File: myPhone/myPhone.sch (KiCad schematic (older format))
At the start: 135 parts, among them J1 USB_OTG, J2 BATT, J3 RV.Debug, J4 SJ-3571N, J5 Display, J6 Touch, Q1 MMBT3906, SW1 RESET, SW2 WAKE, U1 BQ25895, U10 74HC595, U11 ICS-43434, U12 MAX98357A, U13 FT813Q, U14 FAN5333BSX, U2 TPS62293, U3 TPS630250, U4 SN74LVC2G07, U5 E310-G000, U6 IS25LP128-JBLE, U7 74HC00, U8 74HC00, U9 74HC595, X1 SiT1533, Y1 16MHz, Y2 12MHz

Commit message: upgrade to kicad 5; fixed footprints
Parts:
- removed J1: USB_OTG, footprints:USB_Micro-B, symbol USB_OTG
- removed J2: BATT, Pin_Headers:Pin_Header_Straight_1x02_Pitch2.00mm, symbol Conn_01x02
- removed J3: RV.Debug, Pin_Headers:Pin_Header_Straight_1x06_Pitch2.54mm, symbol Conn_01x06
- removed J5: Display, footprints:Hirose_FH12-40S-0.5SH_1x40-1MP_P0.50mm_Horizontal_Bottom, symbol Conn_01x40
- removed J6: Touch, footprints:Hirose_FH12-6S-0.5SH_1x06-1MP_P0.50mm_Horizontal_Bottom, symbol Conn_01x06
- removed Q1: MMBT3906, TO_SOT_Packages_SMD:SOT-23, symbol MMBT3906
- removed SW1: RESET, footprints:Panasonic_EVPBB, symbol SW_Push
- removed SW2: WAKE, footprints:Panasonic_EVPAK, symbol SW_Push
- removed U10, U9: 74HC595, Housings_SOIC:SOIC-16_3.9x9.9mm_Pitch1.27mm, symbol 74HC595
- removed U7, U8: 74HC00, Housings_SOIC:SOIC-14_3.9x8.7mm_Pitch1.27mm, symbol 74HC00
- added J1: USB_OTG, footprints:USB_Micro-B, symbol Connector:USB_B_Micro
- added J2: BATT, Connector_PinHeader_2.00mm:PinHeader_1x02_P2.00mm_Vertical, symbol Connector_Generic:Conn_01x02
- added J3: RV.Debug, Connector_PinHeader_2.54mm:PinHeader_1x06_P2.54mm_Vertical, symbol Connector_Generic:Conn_01x06
- added J5: Display, footprints:Hirose_FH12-40S-0.5SH_1x40-1MP_P0.50mm_Horizontal_Bottom, symbol Connector_Generic:Conn_01x40
- added J6: Touch, footprints:Hirose_FH12-6S-0.5SH_1x06-1MP_P0.50mm_Horizontal_Bottom, symbol Connector_Generic:Conn_01x06
- added Q1: MMBT3906, Package_TO_SOT_SMD:SOT-23, symbol Transistor_BJT:MMBT3906
- added SW1: RESET, footprints:Panasonic_EVPBB, symbol Switch:SW_Push
- added SW2: WAKE, footprints:Panasonic_EVPAK, symbol Switch:SW_Push
- added U10, U9: 74HC595, Package_SO:SOIC-16_3.9x9.9mm_P1.27mm, symbol 74xx:74HC595
- added U7, U8: 74HC00, Package_SO:SOIC-14_3.9x8.7mm_P1.27mm, symbol 74xx:74HC00
- BZ1: symbol Buzzer -> Device:Buzzer
- C1, C10, C11, C2, C29, C3, C30, C31, C32, C33, C34, C35, C36, C37, C4, C48, C49, C5, C50, C51, C52, C53, C54, C6, C7, C8, C9: footprint Capacitors_SMD:C_0603 -> Capacitor_SMD:C_0603_1608Metric; symbol C -> Device:C
- C12, C13, C14, C15, C16, C17, C18, C19, C20, C21, C22, C23, C24, C25, C26, C27, C28, C38, C39, C40, C41, C42, C43, C44, C45, C46, C47: footprint Capacitors_SMD:C_0603 -> Capacitor_SMD:C_0603_1608Metric; symbol C_Small -> Device:C_Small
- D1: footprint LEDs:LED_0603 -> LED_SMD:LED_0603_1608Metric; symbol LED -> Device:LED
- D2: footprint Diodes_SMD:D_SOD-123 -> Diode_SMD:D_SOD-123; symbol D_Schottky -> Device:D_Schottky
- D3: footprint footprints:DO-214AC -> Diode_SMD:D_SMA; symbol D_Zener -> Device:D_Zener
- J4: symbol SJ-3571N -> cui-sj:SJ-3571N
- JP1, JP2, JP3: footprint Pin_Headers:Pin_Header_Straight_1x02_Pitch1.27mm -> Connector_PinHeader_1.27mm:PinHeader_1x02_P1.27mm_Vertical; symbol Jumper -> Device:Jumper
- L1, L2: footprint footprints:Coilcraft_LPS3015 -> footprints:L_Coilcraft_LPS3015; symbol L -> Device:L
- L3: footprint footprints:Coilcraft_XAL40 -> footprints:L_Coilcraft_XAL40; symbol L -> Device:L
- L4: footprint footprints:Murata_LQH66SN -> footprints:L_Murata_LQH66SN; symbol L -> Device:L
- LS1: footprint Pin_Headers:Pin_Header_Straight_1x02_Pitch1.27mm -> Connector_PinHeader_1.27mm:PinHeader_1x02_P1.27mm_Vertical; symbol Speaker -> Device:Speaker
- R1, R10, R11, R12, R13, R14, R15, R16, R17, R18, R19, R2, R20, R21, R22, R23, R24, R25, R26, R27, R28, R29, R3, R31, R32, R33, R34, R35, R4, R5, R6, R7, R8, R9: footprint Resistors_SMD:R_0603 -> Resistor_SMD:R_0603_1608Metric; symbol R -> Device:R
- R30: footprint Resistors_SMD:R_0603 -> Resistor_SMD:R_0603_1608Metric; symbol R_Small -> Device:R_Small
- RN1, RN2, RN3, RN4, RN5, RN6, RN7, RN8: symbol R_Pack04 -> Device:R_Pack04
- U1: footprint footprints:QFN-24-1EP_4x4mm_Pitch0.5mm -> Package_DFN_QFN:Texas_S-PWQFN-N24_EP2.7x2.7mm_ThermalVias; symbol BQ25895 -> texas-tps:BQ25895
- U11: symbol ICS-43434 -> ics-43434:ICS-43434
- U12: footprint footprints:MAX98357 -> Package_DFN_QFN:TQFN-16-1EP_3x3mm_P0.5mm_EP1.23x1.23mm; symbol MAX98357 -> max98357:MAX98357
- U13: footprint footprints:FT813Q -> Package_DFN_QFN:QFN-56-1EP_8x8mm_P0.5mm_EP5.6x5.6mm_ThermalVias; symbol FT813Q -> ft81x:FT813Q
- U14: footprint TO_SOT_Packages_SMD:SOT-23-5 -> Package_TO_SOT_SMD:SOT-23-5; symbol FAN5333 -> fan5333:FAN5333
- U2: symbol TPS62290 -> texas-tps:TPS62290
- U3: symbol TPS630250 -> texas-tps:TPS630250
- U4: footprint TO_SOT_Packages_SMD:SC-70-6 -> Package_TO_SOT_SMD:SOT-363_SC-70-6; symbol SN74LVC2G07 -> sn74:SN74LVC2G07
- U5: footprint Housings_DFN_QFN:UQFN-48-1EP_6x6mm_Pitch0.4mm -> Package_DFN_QFN:QFN-48-1EP_6x6mm_P0.4mm_EP4.2x4.2mm_ThermalVias; symbol E310-G000 -> e310-g000:E310-G000
- U6: footprint Housings_SOIC:SOIJ-8_5.3x5.3mm_Pitch1.27mm -> Package_SO:SOIJ-8_5.3x5.3mm_P1.27mm; symbol IS25LP128 -> is25lp128:IS25LP128
- X1: symbol SiT1533 -> sit1533:SiT1533
- Y1, Y2: symbol Crystal_GND3_Small -> Device:Crystal_GND3_Small
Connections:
- wire segments 582 -> 778
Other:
- moved on the sheet: BZ1, C29, C30, C31, C32, C33, C34, C35, C36, C37, R15, R16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

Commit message: REV1 board
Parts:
- removed C15: 0.1uF, Capacitor_SMD:C_0603_1608Metric, symbol Device:C_Small
- removed J3: RV.Debug, Connector_PinHeader_2.54mm:PinHeader_1x06_P2.54mm_Vertical, symbol Connector_Generic:Conn_01x06
- removed J5: Display, footprints:Hirose_FH12-40S-0.5SH_1x40-1MP_P0.50mm_Horizontal_Bottom, symbol Connector_Generic:Conn_01x40
- removed J6: Touch, footprints:Hirose_FH12-6S-0.5SH_1x06-1MP_P0.50mm_Horizontal_Bottom, symbol Connector_Generic:Conn_01x06
- removed R30: 33R, Resistor_SMD:R_0603_1608Metric, symbol Device:R_Small
- removed R31: 4.7K, Resistor_SMD:R_0603_1608Metric, symbol Device:R
- removed R32, R33: 1K, Resistor_SMD:R_0603_1608Metric, symbol Device:R
- removed R34: 100K, Resistor_SMD:R_0603_1608Metric, symbol Device:R
- removed RN1, RN2, RN3, RN4, RN5, RN6, RN7, RN8: 33R, footprints:R_Array_Convex_4x0402, symbol Device:R_Pack04
- removed U4: SN74LVC2G07, Package_TO_SOT_SMD:SOT-363_SC-70-6, symbol sn74:SN74LVC2G07
- removed U5: E310-G000, Package_DFN_QFN:QFN-48-1EP_6x6mm_P0.4mm_EP4.2x4.2mm_ThermalVias, symbol e310-g000:E310-G000
- added R36: 100K, Resistor_SMD:R_0603_1608Metric, symbol Device:R
- added U5: E310-G002, Package_DFN_QFN:QFN-48-1EP_6x6mm_P0.4mm_EP4.2x4.2mm_ThermalVias, symbol e310-g000:E310-G002
- U10, U9: footprint Package_SO:SOIC-16_3.9x9.9mm_P1.27mm -> footprints:74HC595BQ115
- U12: footprint Package_DFN_QFN:TQFN-16-1EP_3x3mm_P0.5mm_EP1.23x1.23mm -> footprints:TQFN-16-1EP_3x3mm_P0.5mm_EP1.23x1.23mm_ThermalVias
- U7, U8: footprint Package_SO:SOIC-14_3.9x8.7mm_P1.27mm -> footprints:74HC00BQ115
- renumbered C20 to C19, C22 to C20, C23 to C21, C19 to C22, C21 to C23, J4 to J3
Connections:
- net +1V8: now also R12.1, U5.30 (VDD), U5.46 (VDD), U5.6 (VDD); no longer C12.1, C19.1, C23.1, R10.2, R11.2, R12.2, X1.4 (VCC)
- net +3V3: now also C12.1, C19.1, C23.1, R10.2, R11.2, X1.4 (VCC), R36.1, U5.11 (IVDD), U5.12 (OTP_AIVDD), U5.19 (AON_IVDD), U5.23 (AON_VDD), U5.32 (IVDD), U5.47 (IVDD)
- net BL_PWM: no longer U13.28 (BL_PWM)
- net GND: now also U5.21 (AON_PSD_LFCLKSEL), U5.49 (GND)
- net GPIO_0: now also U5.25 (GPIO_0/PWM0.0)
- net GPIO_13: now also U5.37 (GPIO_13/PWM2.3)
- net GPIO_18: now also U5.40 (GPIO_18)
- net GPIO_20: now also U5.42 (GPIO_20/PWM1.0)
- net GPIO_21: now also U5.43 (GPIO_21/PWM1.2)
- net GPIO_22: now also U5.44 (GPIO_22/PWM1.3)
- net GPIO_23: now also U5.45 (GPIO_23)
- net JTAG_TCK: now also U5.13 (JTAG_TCK)
- net JTAG_TDI: now also U5.16 (JTAG_TDI)
- net JTAG_TDO: now also U5.14 (JTAG_TDO)
- net JTAG_TMS: now also U5.15 (JTAG_TMS)
- net PWM0.1: now also U5.26 (GPIO_1/PWM0.1)
- net PWM1.1: now also U5.41 (GPIO_19/PWM1.1)
- net PWM2.1: now also U5.35 (GPIO_11/PWM2.1)
- net PWM2.2: now also U5.36 (GPIO_12/PWM2.2)
- net RESET: now also C13.1, R10.1, SW1.2, U5.24 (AON_ERST_N)
- net SPI1.MISO: now also U5.29 (GPIO_4/SPI1.MISO)
- net SPI1.MOSI: now also U5.28 (GPIO_3/SPI1.MOSI/PWM0.3)
- net SPI1.SCK: now also U5.31 (GPIO_5/SPI1.SCK)
- net SPI1.SS0: now also U5.27 (GPIO_2/SPI1.SS0/PWM0.2)
- net SPI1.SS2: now also U5.33 (GPIO_9/SPI1.SS2)
- net SPI1.SS3: now also U5.34 (GPIO_10/SPI1.SS3/PWM2.0)
- net UART0.RX: now also U5.38 (GPIO_16/UART0.RX)
- net UART0.TX: now also U5.39 (GPIO_17/UART0.TX)
- net WAKE: now also C14.1, R11.1, SW2.1, U5.18 (AON_PMU_DWAKEUP_N)
- net XTAL_XO: now reaches C28.1, Y1.2
- net XTAL_XO: now also U5.10 (16M_XTAL_XO)
- net XTAL_XI: now reaches C27.1, Y1.1
- net XTAL_XI: now also U5.9 (16M_XTAL_XI)
- net PLL_AVDD: now reaches C25.1, C26.1
- net PLL_AVDD: now also R12.2, U5.7 (PLL_AVDD); no longer R12.1
- net PLL_AVSS: now reaches C25.2, C26.2
- net PLL_AVSS: now also U5.8 (PLL_AVSS)
- net QSPI_CS: now reaches R35.2, U6.1 (S#)
- net QSPI_CS: now also U5.5 (QSPI_CS)
- net QSPI_DQ_1: now reaches U6.2 (MISO/IO1)
- net QSPI_DQ_1: now also U5.3 (QSPI_DQ_1)
- net QSPI_DQ_2: now reaches U6.3 (WP#/IO2)
- net QSPI_DQ_2: now also U5.2 (QSPI_DQ_2)
- net QSPI_DQ_0: now reaches U6.5 (MOSI/IO0)
- net QSPI_DQ_0: now also U5.4 (QSPI_DQ_0)
- net QSPI_CLK: now reaches U6.6 (SCK)
- net QSPI_CLK: now also U5.48 (QSPI_CLK)
- net QSPI_DQ_3: now reaches U6.7 (HOLD#/IO3)
- net QSPI_DQ_3: now also R36.2, U5.1 (QSPI_DQ_3)
- net PSD_LFALTCLK: now reaches X1.3 (CLKOUT)
- net PSD_LFALTCLK: now also U5.20 (AON_PSD_LFALTCLK)
- net FT813_R0: now reaches U13.2 (R0)
- net FT813_R1: now reaches U13.1 (R1)
- net FT813_R2: now reaches U13.56 (R2)
- net FT813_R3: now reaches U13.55 (R3)
- net FT813_R4: now reaches U13.54 (R4)
- net FT813_R5: now reaches U13.53 (R5)
- net FT813_R6: now reaches U13.52 (R6)
- net FT813_R7: now reaches U13.51 (R7)
- net FT813_G0: now reaches U13.50 (G0)
- net FT813_G1: now reaches U13.49 (G1)
- net FT813_G2: now reaches U13.48 (G2)
- net FT813_G3: now reaches U13.47 (G3)
- net FT813_G4: now reaches U13.46 (G4)
- net FT813_G5: now reaches U13.45 (G5)
- net FT813_G6: now reaches U13.44 (G6)
- net FT813_G7: now reaches U13.43 (G7)
- net FT813_B0: now reaches U13.41 (B0)
- net FT813_B1: now reaches U13.40 (B1)
- net FT813_B2: now reaches U13.39 (B2)
- net FT813_B3: now reaches U13.38 (B3)
- net FT813_B4: now reaches U13.37 (B4)
- net FT813_B5: now reaches U13.36 (B5)
- net FT813_B6: now reaches U13.35 (B6)
- net FT813_B7: now reaches U13.34 (B7)
- net FT813_DISP: now reaches U13.32 (DISP)
- net FT813_HSYNC: now reaches U13.31 (HSYNC)
- net FT813_VSYNC: now reaches U13.30 (VSYNC)
- net FT813_DE: now reaches U13.29 (DE)
- net FT813_PCLK: now reaches U13.33 (PCLK)
- net CTP_INT renamed FT813_CTP_INT
- net CTP_RST renamed FT813_CTP_RST
- net CTP_SCL renamed FT813_CTP_SCL
- net CTP_SDA renamed FT813_CTP_SDA
- new net FT813_BL_PWM: U13.28 (BL_PWM)
- no-connect marks 33 -> 28
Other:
- moved on the sheet: BZ1, C10, C11, C12, C13, C14, C16, C17, C18, C19, C20, C21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

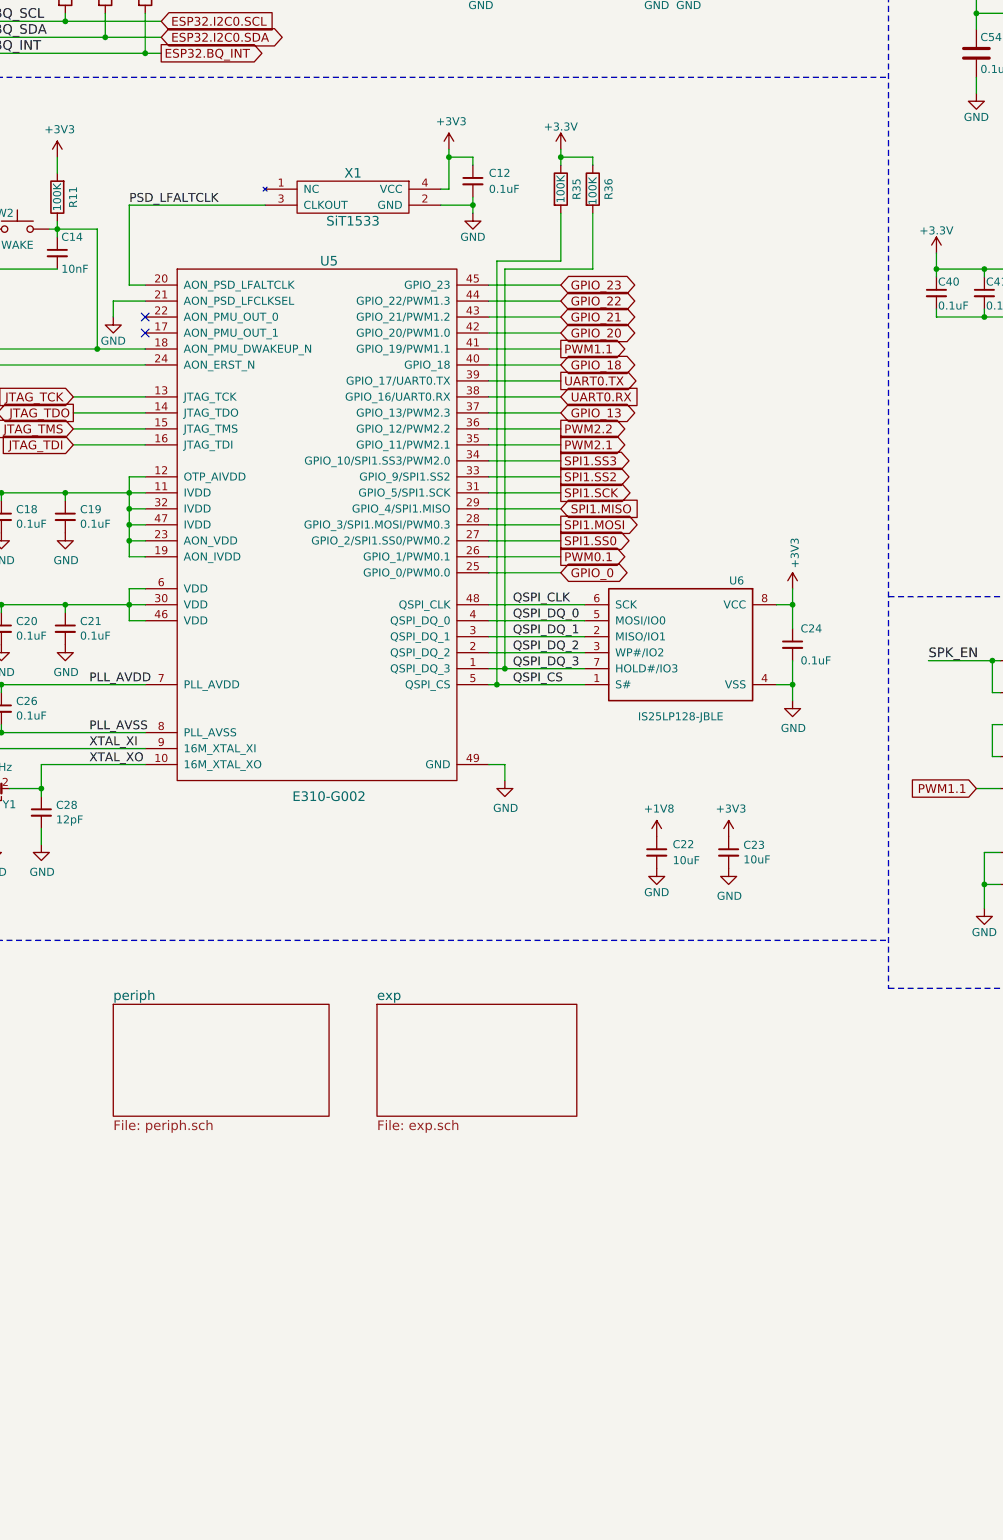
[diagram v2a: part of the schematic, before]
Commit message: display switch pull resistors added
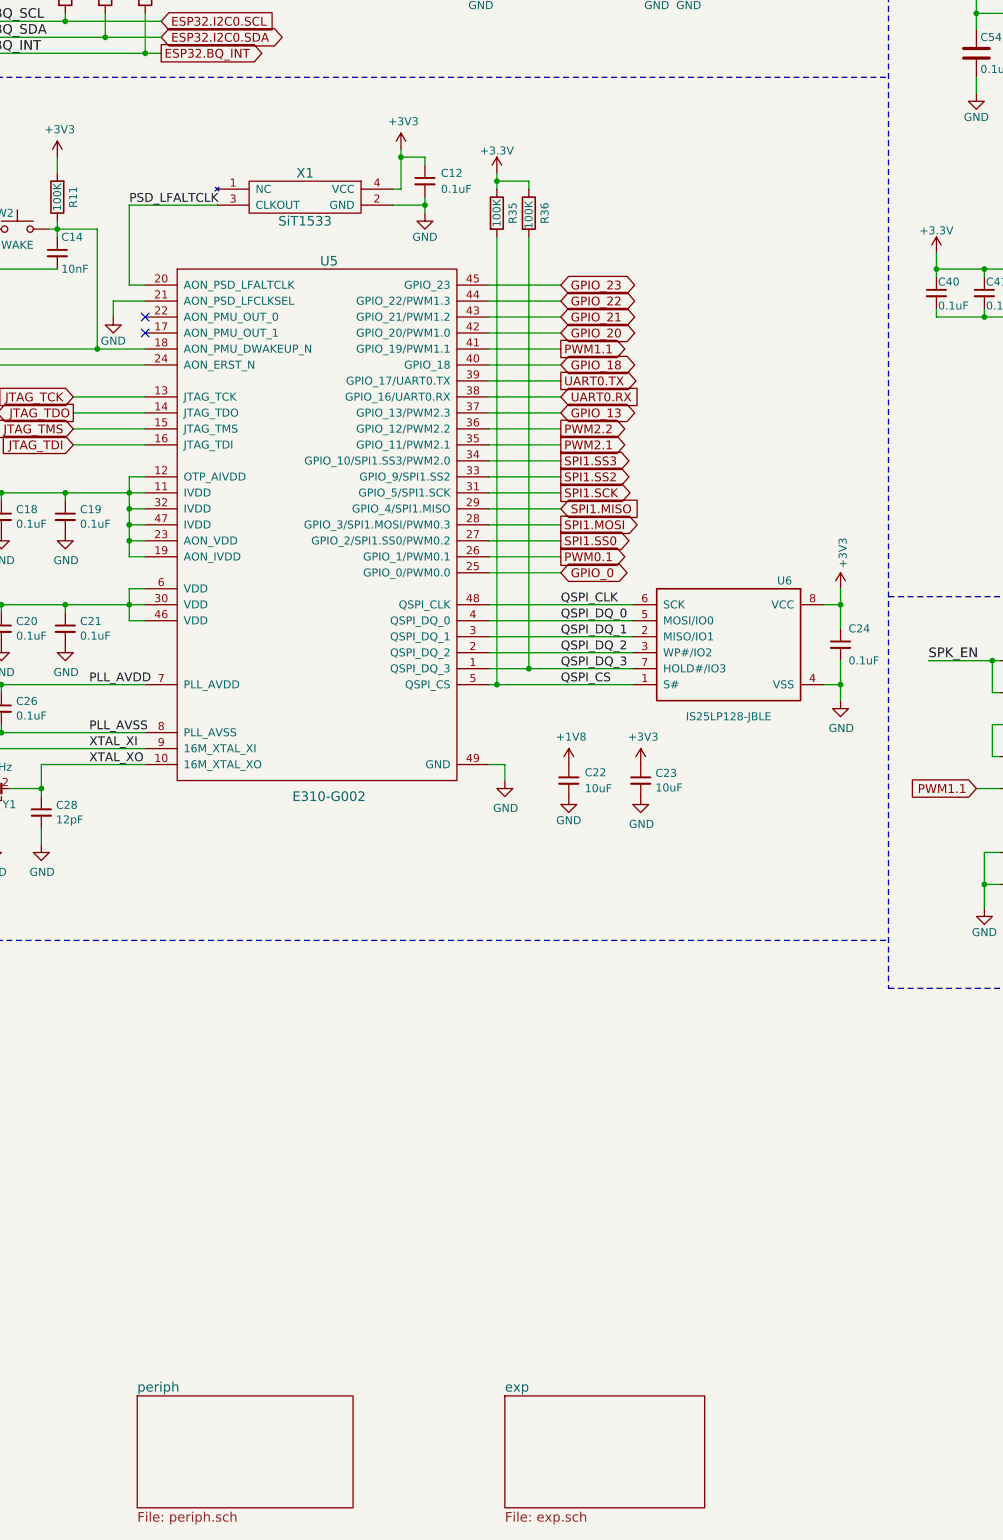
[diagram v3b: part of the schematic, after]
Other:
- moved on the sheet: C12, C22, C23, C24, R35, R36, U6, X1

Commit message: fixed battery charger; added i2c switch for fe310; swapped pwm1/pwm2 for mic/spk
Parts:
- removed JP1: VSYS, Connector_PinHeader_1.27mm:PinHeader_1x02_P1.27mm_Vertical, symbol Device:Jumper
- removed JP2: 3V3, Connector_PinHeader_1.27mm:PinHeader_1x02_P1.27mm_Vertical, symbol Device:Jumper
- removed JP3: 1V8, Connector_PinHeader_1.27mm:PinHeader_1x02_P1.27mm_Vertical, symbol Device:Jumper
- added C15: 0.1uF, Capacitor_SMD:C_0603_1608Metric, symbol Device:C
- added C55, C56: 22uF, Capacitor_SMD:C_0603_1608Metric, symbol Device:C
- added U4: TMUX154E, Package_DFN_QFN:UQFN-10_1.3x1.8mm_P0.4mm, symbol tmux:TMUX154E
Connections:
- net +3V3: now also C15.1, U4.9 (VCC)
- net GND: now also C15.2, C55.2, C56.2, U4.4 (GND), U4.8 (/EN)
- net GPIO_13: now also U4.3 (A); no longer U10.9 (QH'), U12.1 (DIN)
- net GPIO_20: no longer R22.2, U11.6 (SD), U9.14 (SER)
- net PWM1.1: now also U11.1 (WS); no longer U12.14 (LRCLK), U8.10
- net PWM2.1: now also U12.14 (LRCLK), U8.10; no longer U11.1 (WS)
- net SPK_EN: now also U4.10 (SEL)
- net WAKE: now also U1.12 (/QON)
- net at U1.23 (PMID): now also C55.1, C56.1
- net ESP32.BQ_INT renamed ESP32.IO39
- net ESP32.I2C0.SCL renamed TMUX.I2C0.SCL
- net TMUX.I2C0.SCL: now also U4.1 (A0)
- net ESP32.I2C0.SDA renamed TMUX.I2C0.SDA
- net TMUX.I2C0.SDA: now also U4.7 (B0)
- net GPIO_21 renamed PWM1.2
- net PWM1.2: now also R17.2, U7.13, U7.2
- removed net PWM2.2: R17.2, U5.36 (GPIO_12/PWM2.2), U7.13, U7.2
- new net GPIO_12: U4.5 (B), U5.36 (GPIO_12/PWM2.2)
- new net I2S_SD_IN: U10.9 (QH'), U12.1 (DIN), U4.2 (A1)
- new net I2S_SD_OUT: R22.2, U11.6 (SD), U4.6 (B1), U9.14 (SER)
- no-connect marks 28 -> 26
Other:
- moved on the sheet: C1, C2, C3, C4, C5, C6, D1, J1, J2, L1, R1, R2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
